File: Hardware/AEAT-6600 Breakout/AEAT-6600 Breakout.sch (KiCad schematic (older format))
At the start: 9 parts, among them J1 Conn_01x16, U1 AEAT-6600-T16

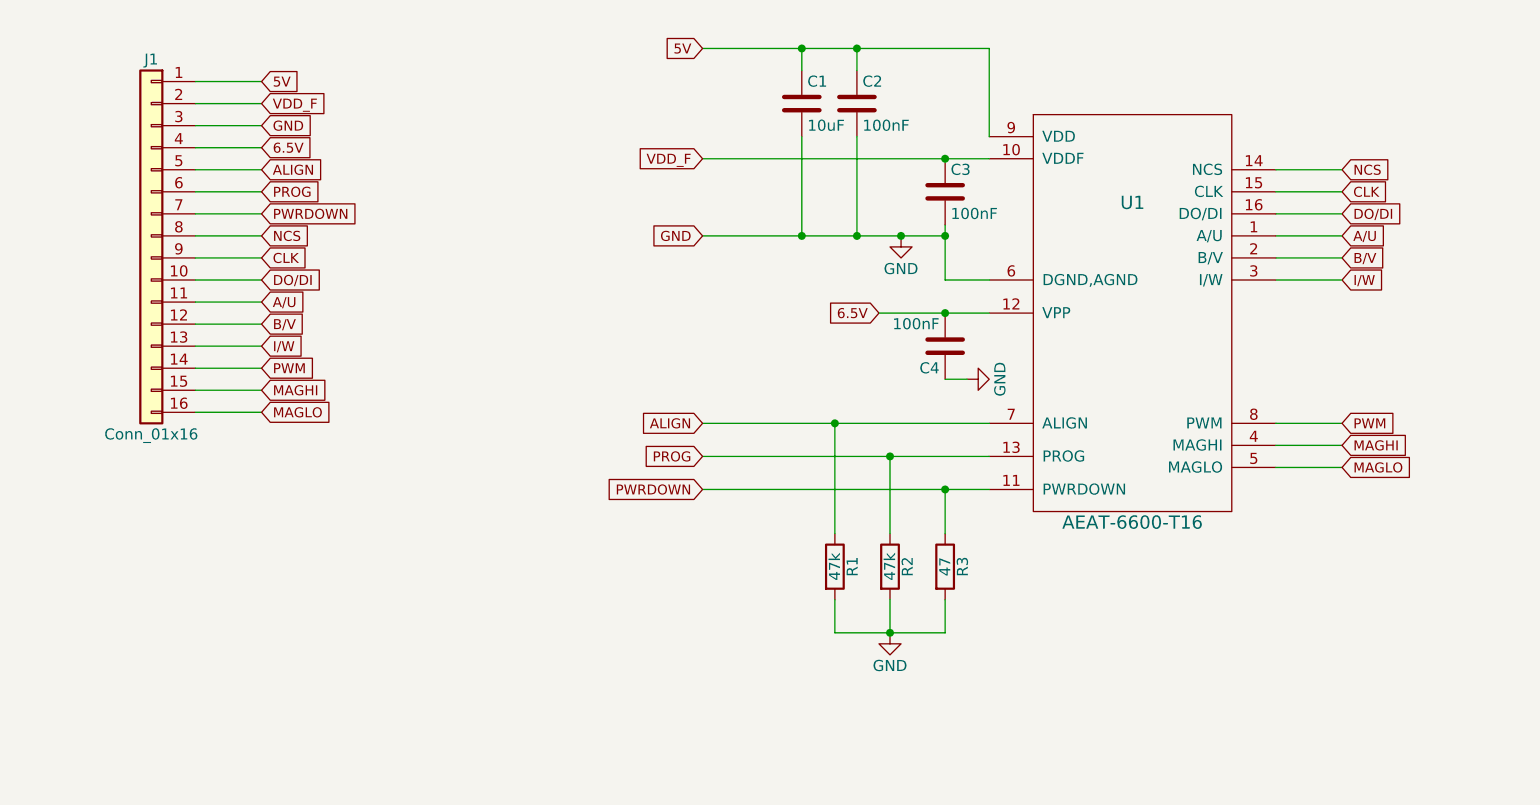
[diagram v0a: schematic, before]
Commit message: Completed AEAT-6600 Breakout
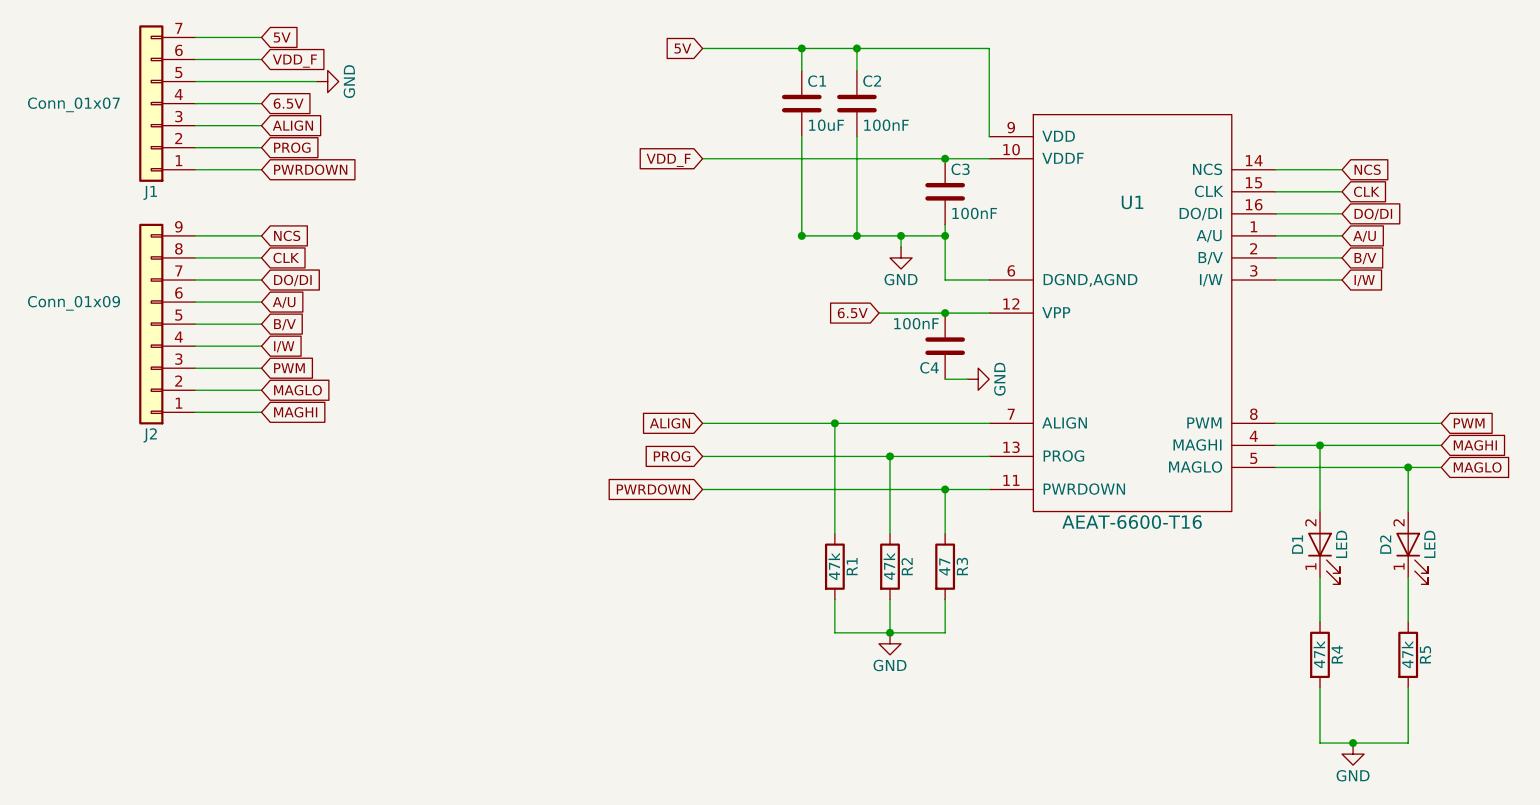
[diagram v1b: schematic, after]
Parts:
- removed J1: Conn_01x16, Pin_Headers:Pin_Header_Angled_1x16_Pitch2.54mm, symbol Conn_01x16
- added D1, D2: LED, LEDs:LED_0603, symbol LED
- added J1: Conn_01x07, Pin_Headers:Pin_Header_Angled_1x07_Pitch2.54mm, symbol Conn_01x07
- added J2: Conn_01x09, Pin_Headers:Pin_Header_Angled_1x09_Pitch2.54mm, symbol Conn_01x09
- added R4, R5: 47k, Resistors_SMD:R_0805, symbol R
- C2: Supplier (none) -> RRRR
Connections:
- net 5V: now also J1.7 (Pin_7)
- net 6.5V: now also J1.4 (Pin_4)
- net A/U: now also J2.6 (Pin_6)
- net ALIGN: now also J1.3 (Pin_3)
- net B/V: now also J2.5 (Pin_5)
- net CLK: now also J2.8 (Pin_8)
- net DO/DI: now also J2.7 (Pin_7)
- net GND: now also J1.5 (Pin_5), R4.2, R5.2
- net I/W: now also J2.4 (Pin_4)
- net MAGHI: now also D1.2 (A), J2.1 (Pin_1)
- net MAGLO: now also D2.2 (A), J2.2 (Pin_2)
- net NCS: now also J2.9 (Pin_9)
- net PROG: now also J1.2 (Pin_2)
- net PWM: now also J2.3 (Pin_3)
- net PWRDOWN: now also J1.1 (Pin_1)
- net VDD_F: now also J1.6 (Pin_6)
- new net: D1.1 (K), R4.1
- new net: D2.1 (K), R5.1
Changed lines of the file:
@@
 LIBS:valves
 LIBS:Avago
+LIBS:AEAT-6600 Breakout-cache
 EELAYER 25 0
 EELAYER END
@@
 $EndDescr
 $Comp
-L AEAT-6600-T16 U1
-U 1 1 5B77B45A
-P 7150 3550
-F 0 "U1" H 7150 4450 60  0000 C CNN
-F 1 "AEAT-6600-T16" H 7150 3000 60  0000 C CNN
-F 2 "Housings_SSOP:TSSOP-16_4.4x5mm_Pitch0.65mm" H 7200 3550 60  0001 C CNN
-F 3 "" H 7200 3550 60  0001 C CNN
-	1    7150 3550
-	1    0    0    -1
-$EndComp
-$Comp
-L Conn_01x16 J1
-U 1 1 5B77B4B2
-P 2700 2800
-F 0 "J1" H 2700 3600 50  0000 C CNN
-F 1 "Conn_01x16" H 2700 1900 50  0000 C CNN
-F 2 "Pin_Headers:Pin_Header_Angled_1x16_Pitch2.54mm" H 2700 2800 50  0001 C CNN
-F 3 "" H 2700 2800 50  0001 C CNN
-	1    2700 2800
-	-1   0    0    -1
-$EndComp
-$Comp
 L C C2
 U 1 1 5B77B526
@@
 F 2 "Capacitors_SMD:C_0805" H 5938 2050 50  0001 C CNN
 F 3 "" H 5900 2200 50  0001 C CNN
+F 4 "RRRR" H 5900 2200 60  0001 C CNN "Supplier"
 	1    5900 2200
 	1    0    0    -1
@@
 L GND #PWR01
 U 1 1 5B77B563
-P 6100 2800
-F 0 "#PWR01" H 6100 2550 50  0001 C CNN
-F 1 "GND" H 6100 2650 50  0000 C CNN
-F 2 "" H 6100 2800 50  0001 C CNN
-F 3 "" H 6100 2800 50  0001 C CNN
-	1    6100 2800
+P 6100 2850
+F 0 "#PWR01" H 6100 2600 50  0001 C CNN
+F 1 "GND" H 6100 2700 50  0000 C CNN
+F 2 "" H 6100 2850 50  0001 C CNN
+F 3 "" H 6100 2850 50  0001 C CNN
+	1    6100 2850
 	1    0    0    -1
 $EndComp
@@
 	0    -1   -1   0
 $EndComp
-Wire Wire Line
-	5200 1950 6500 1950
 $Comp
 L C C4
@@
 	-1   0    0    1
 $EndComp
-Wire Wire Line
-	5200 2800 6300 2800
-Wire Wire Line
-	6300 2750 6300 3000
-Connection ~ 6100 2800
-Wire Wire Line
-	5200 2450 6500 2450
-Wire Wire Line
-	6500 1950 6500 2350
-Wire Wire Line
-	5900 2350 5900 2800
-Wire Wire Line
-	5900 1950 5900 2050
 $Comp
 L C C1
@@
 	1    0    0    -1
 $EndComp
-Wire Wire Line
-	5650 2350 5650 2800
-Connection ~ 5900 2800
-Wire Wire Line
-	5650 2050 5650 1950
-Connection ~ 5900 1950
-Connection ~ 6300 2450
-Connection ~ 5650 1950
-Wire Wire Line
-	6300 3000 6500 3000
-Connection ~ 6300 2800
-Connection ~ 5650 2800
-Text GLabel 5200 2800 0    45   Input ~ 0
-GND
 Text GLabel 6000 3150 0    45   Input ~ 0
 6.5V
-Wire Wire Line
-	6000 3150 6500 3150
-Connection ~ 6300 3150
-Wire Wire Line
-	6300 3450 6400 3450
 Text GLabel 5200 1950 0    45   Input ~ 0
 5V
@@
 	1    0    0    -1
 $EndComp
-Wire Wire Line
-	5200 3950 6500 3950
-Wire Wire Line
-	6300 3950 6300 4150
-Wire Wire Line
-	5200 3800 6500 3800
-Wire Wire Line
-	6050 3800 6050 4150
-Wire Wire Line
-	5200 3650 6500 3650
-Wire Wire Line
-	5800 3650 5800 4150
 $Comp
 L GND #PWR03
 U 1 1 5B77BE89
-P 6050 4600
-F 0 "#PWR03" H 6050 4350 50  0001 C CNN
-F 1 "GND" H 6050 4450 50  0000 C CNN
-F 2 "" H 6050 4600 50  0001 C CNN
-F 3 "" H 6050 4600 50  0001 C CNN
-	1    6050 4600
-	1    0    0    -1
-$EndComp
-Wire Wire Line
-	5800 4450 5800 4600
-Wire Wire Line
-	5800 4600 6300 4600
-Wire Wire Line
-	6050 4600 6050 4450
-Wire Wire Line
-	6300 4600 6300 4450
-Connection ~ 6050 4600
-Connection ~ 5800 3650
-Connection ~ 6050 3800
-Connection ~ 6300 3950
+P 8150 5100
+F 0 "#PWR03" H 8150 4850 50  0001 C CNN
+F 1 "GND" H 8150 4950 50  0000 C CNN
+F 2 "" H 8150 5100 50  0001 C CNN
+F 3 "" H 8150 5100 50  0001 C CNN
+	1    8150 5100
+	1    0    0    -1
+$EndComp
 Text GLabel 5200 3650 0    45   Input ~ 0
 ALIGN
@@
 Text GLabel 8100 3000 2    45   Input ~ 0
 I/W
-Text GLabel 8100 3650 2    45   Input ~ 0
+Text GLabel 8550 3650 2    45   Input ~ 0
 PWM
-Text GLabel 8100 3750 2    45   Input ~ 0
+Text GLabel 8550 3750 2    45   Input ~ 0
 MAGHI
-Text GLabel 8100 3850 2    45   Input ~ 0
+Text GLabel 8550 3850 2    45   Input ~ 0
 MAGLO
-Wire Wire Line
-	7800 2500 8100 2500
-Wire Wire Line
-	8100 2600 7800 2600
-Wire Wire Line
-	7800 2700 8100 2700
-Wire Wire Line
-	8100 2800 7800 2800
-Wire Wire Line
-	7800 2900 8100 2900
-Wire Wire Line
-	8100 3000 7800 3000
-Wire Wire Line
-	7800 3650 8100 3650
-Wire Wire Line
-	8100 3750 7800 3750
-Wire Wire Line
-	7800 3850 8100 3850
-Text GLabel 3200 2100 2    45   Input ~ 0
+Text GLabel 3200 1900 2    45   Input ~ 0
 5V
+Text GLabel 3200 2000 2    45   Input ~ 0
+VDD_F
+Text GLabel 3200 2200 2    45   Input ~ 0
+6.5V
 Text GLabel 3200 2300 2    45   Input ~ 0
-GND
-Text GLabel 3200 2200 2    45   Input ~ 0
-VDD_F
+ALIGN
 Text GLabel 3200 2400 2    45   Input ~ 0
-6.5V
+PROG
 Text GLabel 3200 2500 2    45   Input ~ 0
-ALIGN
-Text GLabel 3200 2600 2    45   Input ~ 0
-PROG
-Text GLabel 3200 2700 2    45   Input ~ 0
 PWRDOWN
 Text GLabel 3200 2800 2    45   Input ~ 0
@@
 Text GLabel 3200 3400 2    45   Input ~ 0
 PWM
+Text GLabel 3200 3600 2    45   Input ~ 0
+MAGHI
 Text GLabel 3200 3500 2    45   Input ~ 0
-MAGHI
-Text GLabel 3200 3600 2    45   Input ~ 0
 MAGLO
-Wire Wire Line
-	2900 2100 3200 2100
+$Comp
+L Conn_01x07 J1
+U 1 1 5B77C0E9
+P 2700 2200
+F 0 "J1" H 2700 2600 50  0000 C CNN
+F 1 "Conn_01x07" H 3050 2200 50  0000 C CNN
+F 2 "Pin_Headers:Pin_Header_Angled_1x07_Pitch2.54mm" H 2700 2200 50  0001 C CNN
+F 3 "" H 2700 2200 50  0001 C CNN
+	1    2700 2200
+	-1   0    0    1
+$EndComp
+$Comp
+L Conn_01x09 J2
+U 1 1 5B77C16A
+P 2700 3200
+F 0 "J2" H 2700 3700 50  0000 C CNN
+F 1 "Conn_01x09" H 3050 3100 50  0000 C CNN
+F 2 "Pin_Headers:Pin_Header_Angled_1x09_Pitch2.54mm" H 2700 3200 50  0001 C CNN
+F 3 "" H 2700 3200 50  0001 C CNN
+	1    2700 3200
+	-1   0    0    1
+$EndComp
+$Comp
+L R R4
+U 1 1 5B77C9AF
+P 8000 4700
+F 0 "R4" V 8080 4700 50  0000 C CNN
+F 1 "47k" V 8000 4700 50  0000 C CNN
+F 2 "Resistors_SMD:R_0805" V 7930 4700 50  0001 C CNN
+F 3 "" H 8000 4700 50  0001 C CNN
+	1    8000 4700
+	1    0    0    -1
+$EndComp
+$Comp
+L R R5
+U 1 1 5B77C9ED
+P 8400 4700
+F 0 "R5" V 8480 4700 50  0000 C CNN
+F 1 "47k" V 8400 4700 50  0000 C CNN
+F 2 "Resistors_SMD:R_0805" V 8330 4700 50  0001 C CNN
+F 3 "" H 8400 4700 50  0001 C CNN
+	1    8400 4700
+	1    0    0    -1
+$EndComp
+$Comp
+L GND #PWR04
+U 1 1 5B77CB69
+P 6050 4600
+F 0 "#PWR04" H 6050 4350 50  0001 C CNN
+F 1 "GND" H 6050 4450 50  0000 C CNN
+F 2 "" H 6050 4600 50  0001 C CNN
+F 3 "" H 6050 4600 50  0001 C CNN
+	1    6050 4600
+	1    0    0    -1
+$EndComp
+$Comp
+L LED D1
+U 1 1 5B77CDA3
+P 8000 4200
+F 0 "D1" H 8000 4300 50  0000 C CNN
+F 1 "LED" H 8000 4100 50  0000 C CNN
+F 2 "LEDs:LED_0603" H 8000 4200 50  0001 C CNN
+F 3 "" H 8000 4200 50  0001 C CNN
+	1    8000 4200
+	0    -1   -1   0
+$EndComp
+$Comp
+L LED D2
+U 1 1 5B77CDEE
+P 8400 4200
+F 0 "D2" H 8400 4300 50  0000 C CNN
+F 1 "LED" H 8400 4100 50  0000 C CNN
+F 2 "LEDs:LED_0603" H 8400 4200 50  0001 C CNN
+F 3 "" H 8400 4200 50  0001 C CNN
+	1    8400 4200
+	0    -1   -1   0
+$EndComp
+$Comp
+L AEAT-6600-T16 U1
+U 1 1 5B77B45A
+P 7150 3550
+F 0 "U1" H 7150 4450 60  0000 C CNN
+F 1 "AEAT-6600-T16" H 7150 3000 60  0000 C CNN
+F 2 "Housings_SSOP:TSSOP-16_4.4x5mm_Pitch0.65mm" H 7200 3550 60  0001 C CNN
+F 3 "" H 7200 3550 60  0001 C CNN
+	1    7150 3550
+	1    0    0    -1
+$EndComp
+Wire Wire Line
+	5200 1950 6500 1950
+Wire Wire Line
+	6300 2750 6300 3000
+Wire Wire Line
+	5200 2450 6500 2450
+Wire Wire Line
+	6500 1950 6500 2350
+Wire Wire Line
+	5900 2350 5900 2800
+Wire Wire Line
+	5900 1950 5900 2050
+Wire Wire Line
+	5650 2350 5650 2800
+Connection ~ 5900 2800
+Wire Wire Line
+	5650 2050 5650 1950
+Connection ~ 5900 1950
+Connection ~ 6300 2450
+Connection ~ 5650 1950
+Wire Wire Line
+	6300 3000 6500 3000
+Connection ~ 6300 2800
+Connection ~ 5650 2800
+Wire Wire Line
+	6000 3150 6500 3150
+Connection ~ 6300 3150
+Wire Wire Line
+	6300 3450 6400 3450
+Wire Wire Line
+	5200 3950 6500 3950
+Wire Wire Line
+	6300 3950 6300 4150
+Wire Wire Line
+	5200 3800 6500 3800
+Wire Wire Line
+	6050 3800 6050 4150
+Wire Wire Line
+	5200 3650 6500 3650
+Wire Wire Line
+	5800 3650 5800 4150
+Wire Wire Line
+	8400 5100 8400 4850
+Connection ~ 8150 5100
+Connection ~ 5800 3650
+Connection ~ 6050 3800
+Connection ~ 6300 3950
+Wire Wire Line
+	7800 2500 8100 2500
+Wire Wire Line
+	8100 2600 7800 2600
+Wire Wire Line
+	7800 2700 8100 2700
+Wire Wire Line
+	8100 2800 7800 2800
+Wire Wire Line
+	7800 2900 8100 2900
+Wire Wire Line
+	8100 3000 7800 3000
+Wire Wire Line
+	7800 3650 8550 3650
+Wire Wire Line
+	7800 3750 8550 3750
+Wire Wire Line
+	7800 3850 8550 3850
+Wire Wire Line
+	2900 1900 3200 1900
+Wire Wire Line
+	2900 2000 3200 2000
+Wire Wire Line
+	2900 2100 3450 2100
 Wire Wire Line
 	2900 2200 3200 2200
 Wire Wire Line
-	3200 2300 2900 2300
-Wire Wire Line
-	2900 2400 3200 2400
+	2900 2300 3200 2300
+Wire Wire Line
+	3200 2400 2900 2400
 Wire Wire Line
 	2900 2500 3200 2500
 Wire Wire Line
-	3200 2600 2900 2600
-Wire Wire Line
-	2900 2700 3200 2700
-Wire Wire Line
 	3200 2800 2900 2800
 Wire Wire Line
@@
 Wire Wire Line
 	3200 3600 2900 3600
+Connection ~ 8400 3850
+Wire Wire Line
+	5800 4450 5800 4600
+Wire Wire Line
+	5800 4600 6300 4600
+Wire Wire Line
+	6050 4600 6050 4450
+Wire Wire Line
+	6300 4600 6300 4450
+Connection ~ 6050 4600
+Wire Wire Line
+	8000 5100 8400 5100
+Wire Wire Line
+	8000 5100 8000 4850
+Wire Wire Line
+	8000 4550 8000 4350
+Wire Wire Line
+	8000 3750 8000 4050
+Wire Wire Line
+	8400 3850 8400 4050
+Wire Wire Line
+	8400 4350 8400 4550
+Connection ~ 8000 3750
+Wire Wire Line
+	5650 2800 6300 2800
+$Comp
+L GND #PWR05
+U 1 1 5B77D87A
+P 3450 2100
+F 0 "#PWR05" H 3450 1850 50  0001 C CNN
+F 1 "GND" H 3450 1950 50  0000 C CNN
+F 2 "" H 3450 2100 50  0001 C CNN
+F 3 "" H 3450 2100 50  0001 C CNN
+	1    3450 2100
+	0    -1   -1   0
+$EndComp
+Wire Wire Line
+	6100 2850 6100 2800
+Connection ~ 6100 2800
 $EndSCHEMATC
